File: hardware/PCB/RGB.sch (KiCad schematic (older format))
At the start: 24 parts, among them U1 IS31FL3733-QFLS4-TR, U2 IS31FL3733-QFLS4-TR

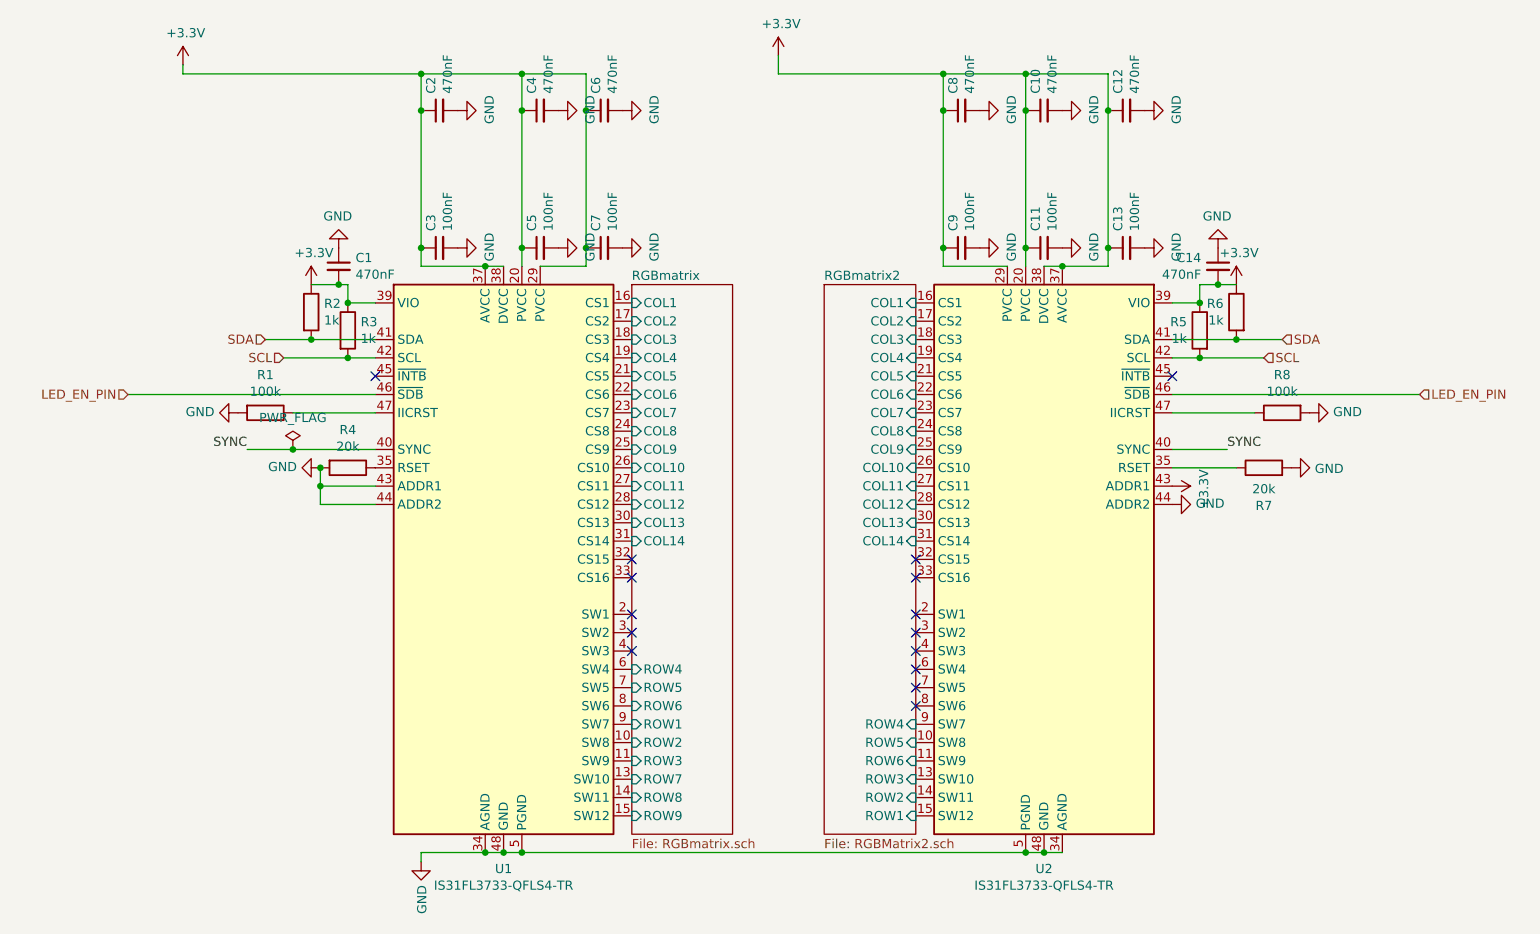
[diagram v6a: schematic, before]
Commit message: fix major issues about the I2C pull up, add in debug
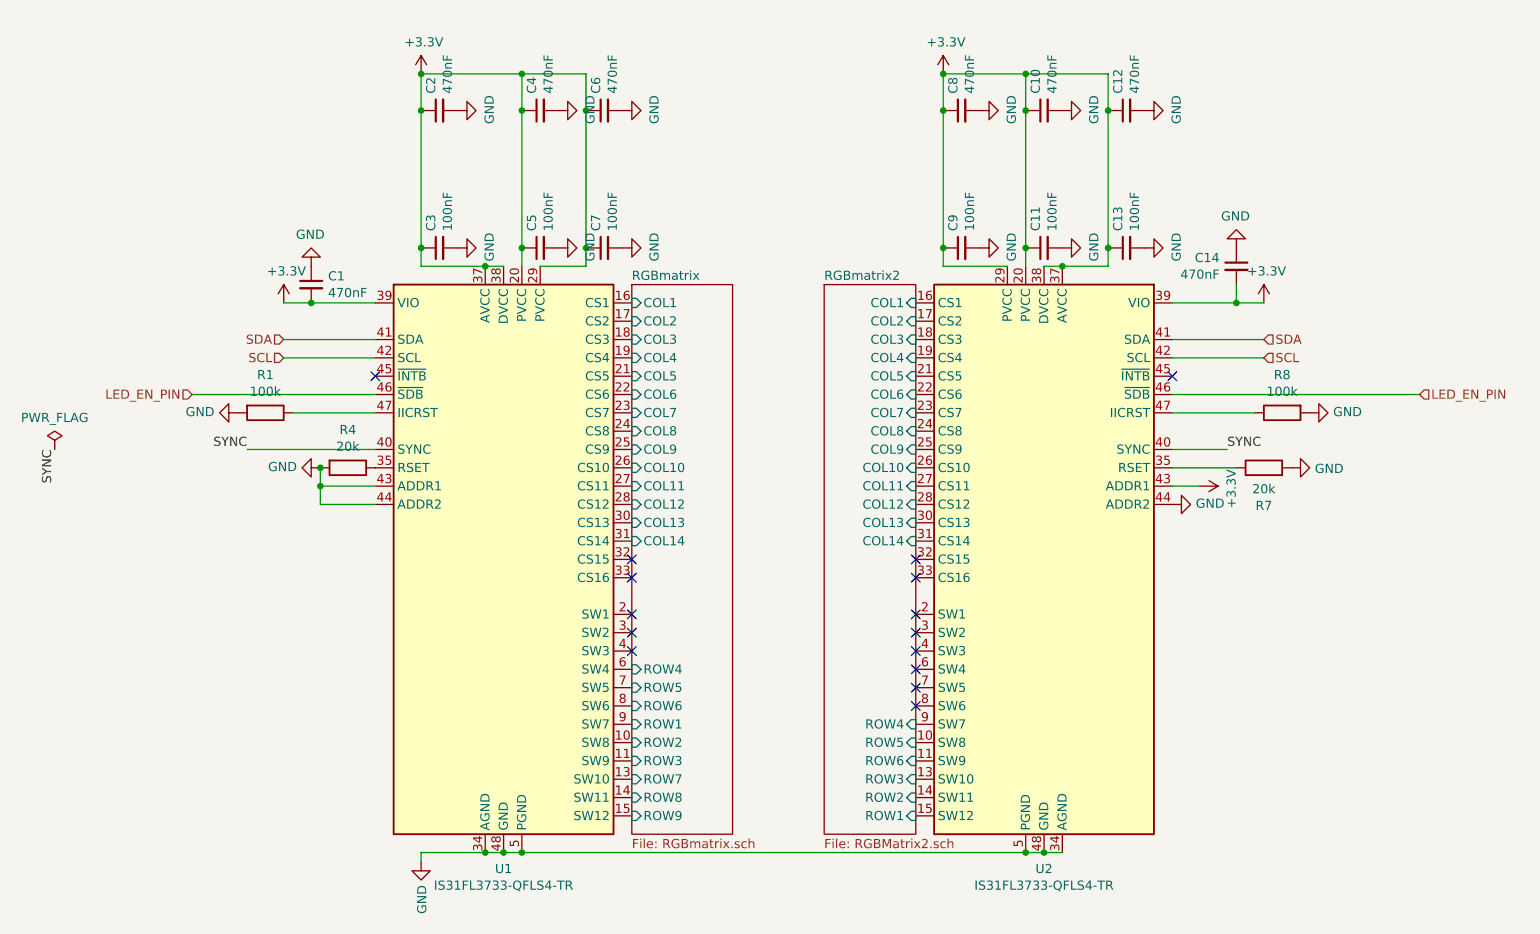
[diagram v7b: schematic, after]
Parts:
- removed R2, R3, R5, R6: 1k, Resistor_SMD:R_0402_1005Metric, symbol Device:R
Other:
- moved on the sheet: C1, C14
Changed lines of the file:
@@
 Text HLabel 8300 2500 2    50   Input ~ 0
 SCL
-Text HLabel 8400 2400 2    50   Input ~ 0
+Text HLabel 8300 2400 2    50   Input ~ 0
 SDA
-Wire Wire Line
-	8400 2400 8150 2400
-Wire Wire Line
-	8150 2400 7800 2400
 Text HLabel 2950 2500 0    50   Input ~ 0
 SCL
-Text HLabel 2850 2400 0    50   Input ~ 0
+Text HLabel 2950 2400 0    50   Input ~ 0
 SDA
 $Comp
@@
 L power:GND #PWR05
 U 1 1 5E42BB66
-P 3250 1900
-F 0 "#PWR05" H 3250 1650 50  0001 C CNN
-F 1 "GND" H 3255 1727 50  0000 C CNN
-F 2 "" H 3250 1900 50  0001 C CNN
-F 3 "" H 3250 1900 50  0001 C CNN
-	1    3250 1900
+P 3100 2000
+F 0 "#PWR05" H 3100 1750 50  0001 C CNN
+F 1 "GND" H 3105 1827 50  0000 C CNN
+F 2 "" H 3100 2000 50  0001 C CNN
+F 3 "" H 3100 2000 50  0001 C CNN
+	1    3100 2000
 	-1   0    0    1
 $EndComp
@@
 L power:GND #PWR022
 U 1 1 5E42518F
-P 8050 1900
-F 0 "#PWR022" H 8050 1650 50  0001 C CNN
-F 1 "GND" H 8055 1727 50  0000 C CNN
-F 2 "" H 8050 1900 50  0001 C CNN
-F 3 "" H 8050 1900 50  0001 C CNN
-	1    8050 1900
+P 8150 1900
+F 0 "#PWR022" H 8150 1650 50  0001 C CNN
+F 1 "GND" H 8155 1727 50  0000 C CNN
+F 2 "" H 8150 1900 50  0001 C CNN
+F 3 "" H 8150 1900 50  0001 C CNN
+	1    8150 1900
 	-1   0    0    1
 $EndComp
@@
 L Device:C_Small C14
 U 1 1 5E406F19
-P 8050 2000
-F 0 "C14" H 8142 2046 50  0000 L CNN
-F 1 "470nF" H 8142 1955 50  0000 L CNN
-F 2 "Capacitor_SMD:C_0402_1005Metric" H 8050 2000 50  0001 C CNN
-F 3 "~" H 8050 2000 50  0001 C CNN
-	1    8050 2000
+P 8150 2000
+F 0 "C14" H 8242 2046 50  0000 L CNN
+F 1 "470nF" H 8242 1955 50  0000 L CNN
+F 2 "Capacitor_SMD:C_0402_1005Metric" H 8150 2000 50  0001 C CNN
+F 3 "~" H 8150 2000 50  0001 C CNN
+	1    8150 2000
 	-1   0    0    -1
 $EndComp
-Connection ~ 7950 2200
-Wire Wire Line
-	7950 2200 7800 2200
-Wire Wire Line
-	7950 2100 7950 2200
-Wire Wire Line
-	8150 2100 8050 2100
-Wire Wire Line
-	7950 2500 8300 2500
-Connection ~ 7950 2500
-$Comp
-L Device:R R5
-U 1 1 5E406F08
-P 7950 2350
-F 0 "R5" H 8020 2396 50  0000 L CNN
-F 1 "1k" H 8020 2305 50  0000 L CNN
-F 2 "Resistor_SMD:R_0402_1005Metric" V 7880 2350 50  0001 C CNN
-F 3 "~" H 7950 2350 50  0001 C CNN
-	1    7950 2350
-	-1   0    0    -1
-$EndComp
-Connection ~ 8150 2400
-$Comp
-L Device:R R6
-U 1 1 5E406EFC
-P 8150 2250
-F 0 "R6" H 8220 2296 50  0000 L CNN
-F 1 "1k" H 8220 2205 50  0000 L CNN
-F 2 "Resistor_SMD:R_0402_1005Metric" V 8080 2250 50  0001 C CNN
-F 3 "~" H 8150 2250 50  0001 C CNN
-	1    8150 2250
-	-1   0    0    -1
-$EndComp
-Wire Wire Line
-	7800 2500 7950 2500
 NoConn ~ 7800 2600
 Wire Wire Line
@@
 NoConn ~ 6400 3700
 NoConn ~ 4850 3700
-Wire Wire Line
-	3250 2100 3300 2100
-Connection ~ 3250 2100
+Connection ~ 3100 2200
 $Comp
 L Device:C_Small C1
 U 1 1 5E39D02A
-P 3250 2000
-F 0 "C1" H 3342 2046 50  0000 L CNN
-F 1 "470nF" H 3342 1955 50  0000 L CNN
-F 2 "Capacitor_SMD:C_0402_1005Metric" H 3250 2000 50  0001 C CNN
-F 3 "~" H 3250 2000 50  0001 C CNN
-	1    3250 2000
+P 3100 2100
+F 0 "C1" H 3192 2146 50  0000 L CNN
+F 1 "470nF" H 3192 2055 50  0000 L CNN
+F 2 "Capacitor_SMD:C_0402_1005Metric" H 3100 2100 50  0001 C CNN
+F 3 "~" H 3100 2100 50  0001 C CNN
+	1    3100 2100
 	1    0    0    -1
 $EndComp
-Connection ~ 3300 2200
-Wire Wire Line
-	3300 2200 3450 2200
 Wire Wire Line
 	4150 5200 4050 5200
@@
 $EndComp
 Wire Wire Line
-	3300 2100 3300 2200
-Wire Wire Line
-	3100 2100 3250 2100
-$Comp
-L Device:R R3
-U 1 1 5E3993FB
-P 3300 2350
-F 0 "R3" H 3370 2396 50  0000 L CNN
-F 1 "1k" H 3370 2305 50  0000 L CNN
-F 2 "Resistor_SMD:R_0402_1005Metric" V 3230 2350 50  0001 C CNN
-F 3 "~" H 3300 2350 50  0001 C CNN
-	1    3300 2350
-	1    0    0    -1
-$EndComp
-$Comp
-L Device:R R2
-U 1 1 5E398E31
-P 3100 2250
-F 0 "R2" H 3170 2296 50  0000 L CNN
-F 1 "1k" H 3170 2205 50  0000 L CNN
-F 2 "Resistor_SMD:R_0402_1005Metric" V 3030 2250 50  0001 C CNN
-F 3 "~" H 3100 2250 50  0001 C CNN
-	1    3100 2250
-	1    0    0    -1
-$EndComp
+	2950 2200 3100 2200
 NoConn ~ 3450 2600
 Wire Wire Line
@@
 Wire Wire Line
 	4600 2000 4350 2000
-Text HLabel 2100 2700 0    50   Input ~ 0
+Text HLabel 2450 2700 0    50   Input ~ 0
 LED_EN_PIN
 Text HLabel 9150 2700 2    50   Input ~ 0
 LED_EN_PIN
-Wire Wire Line
-	3450 2400 3100 2400
-Connection ~ 3100 2400
-Wire Wire Line
-	3100 2400 2850 2400
-Wire Wire Line
-	2950 2500 3300 2500
-Connection ~ 3300 2500
-Wire Wire Line
-	3300 2500 3450 2500
-Wire Wire Line
-	5650 950  6550 950
 Text Label 2750 3000 2    50   ~ 0
 SYNC
@@
 Wire Wire Line
 	8100 3000 7800 3000
-Wire Wire Line
-	2750 3000 3000 3000
 $Comp
 L power:PWR_FLAG #FLG01
 U 1 1 5E6BEB0B
-P 3000 3000
-F 0 "#FLG01" H 3000 3075 50  0001 C CNN
-F 1 "PWR_FLAG" H 3000 3173 50  0000 C CNN
-F 2 "" H 3000 3000 50  0001 C CNN
-F 3 "~" H 3000 3000 50  0001 C CNN
-	1    3000 3000
+P 1700 3000
+F 0 "#FLG01" H 1700 3075 50  0001 C CNN
+F 1 "PWR_FLAG" H 1700 3173 50  0000 C CNN
+F 2 "" H 1700 3000 50  0001 C CNN
+F 3 "~" H 1700 3000 50  0001 C CNN
+	1    1700 3000
 	1    0    0    -1
 $EndComp
-Connection ~ 3000 3000
-Wire Wire Line
-	3000 3000 3450 3000
-Wire Wire Line
-	5650 850  5650 950
-Wire Wire Line
-	2400 900  2400 950
-Connection ~ 3700 950
 Connection ~ 3700 1900
 Wire Wire Line
@@
 Wire Wire Line
 	4600 1150 4600 1900
-Wire Wire Line
-	2400 950  3700 950
 Connection ~ 6550 1900
 Wire Wire Line
@@
 Wire Wire Line
 	7450 1900 7450 2000
-Connection ~ 8050 2100
-Wire Wire Line
-	7950 2100 8050 2100
 Wire Wire Line
 	8150 3100 7800 3100
@@
 	7450 1150 7450 1900
 $Comp
-L power:+3.3V #PWR01
-U 1 1 5E275074
-P 2400 900
-F 0 "#PWR01" H 2400 750 50  0001 C CNN
-F 1 "+3.3V" H 2415 1073 50  0000 C CNN
-F 2 "" H 2400 900 50  0001 C CNN
-F 3 "" H 2400 900 50  0001 C CNN
-	1    2400 900
-	1    0    0    -1
-$EndComp
-$Comp
 L power:+3.3V #PWR03
 U 1 1 5E277141
-P 3100 2100
-F 0 "#PWR03" H 3100 1950 50  0001 C CNN
-F 1 "+3.3V" H 3115 2273 50  0000 C CNN
-F 2 "" H 3100 2100 50  0001 C CNN
-F 3 "" H 3100 2100 50  0001 C CNN
-	1    3100 2100
+P 2950 2200
+F 0 "#PWR03" H 2950 2050 50  0001 C CNN
+F 1 "+3.3V" H 2965 2373 50  0000 C CNN
+F 2 "" H 2950 2200 50  0001 C CNN
+F 3 "" H 2950 2200 50  0001 C CNN
+	1    2950 2200
 	1    0    0    -1
 $EndComp
@@
 L power:+3.3V #PWR013
 U 1 1 5E27A2F2
-P 5650 850
-F 0 "#PWR013" H 5650 700 50  0001 C CNN
-F 1 "+3.3V" H 5665 1023 50  0000 C CNN
-F 2 "" H 5650 850 50  0001 C CNN
-F 3 "" H 5650 850 50  0001 C CNN
-	1    5650 850
+P 6550 950
+F 0 "#PWR013" H 6550 800 50  0001 C CNN
+F 1 "+3.3V" H 6565 1123 50  0000 C CNN
+F 2 "" H 6550 950 50  0001 C CNN
+F 3 "" H 6550 950 50  0001 C CNN
+	1    6550 950
 	1    0    0    -1
 $EndComp
@@
 L power:+3.3V #PWR023
 U 1 1 5E27D7A3
-P 8150 2100
-F 0 "#PWR023" H 8150 1950 50  0001 C CNN
-F 1 "+3.3V" H 8165 2273 50  0000 C CNN
-F 2 "" H 8150 2100 50  0001 C CNN
-F 3 "" H 8150 2100 50  0001 C CNN
-	1    8150 2100
+P 8300 2200
+F 0 "#PWR023" H 8300 2050 50  0001 C CNN
+F 1 "+3.3V" H 8315 2373 50  0000 C CNN
+F 2 "" H 8300 2200 50  0001 C CNN
+F 3 "" H 8300 2200 50  0001 C CNN
+	1    8300 2200
 	1    0    0    -1
 $EndComp
@@
 L power:+3.3V #PWR020
 U 1 1 5E280F4E
-P 7800 3200
-F 0 "#PWR020" H 7800 3050 50  0001 C CNN
-F 1 "+3.3V" H 7815 3373 50  0000 C CNN
-F 2 "" H 7800 3200 50  0001 C CNN
-F 3 "" H 7800 3200 50  0001 C CNN
-	1    7800 3200
+P 7950 3200
+F 0 "#PWR020" H 7950 3050 50  0001 C CNN
+F 1 "+3.3V" H 7965 3373 50  0000 C CNN
+F 2 "" H 7950 3200 50  0001 C CNN
+F 3 "" H 7950 3200 50  0001 C CNN
+	1    7950 3200
 	0    1    1    0
 $EndComp
@@
 Wire Wire Line
 	7800 2700 9150 2700
-Wire Wire Line
-	2100 2700 3450 2700
 NoConn ~ 4850 4100
 NoConn ~ 4850 4000
@@
 F21 "ROW6" I R 6400 4700 50
 $EndSheet
+Wire Wire Line
+	2950 2500 3450 2500
+Wire Wire Line
+	7950 3200 7800 3200
+Wire Wire Line
+	3450 2400 2950 2400
+Wire Wire Line
+	7800 2500 8300 2500
+Wire Wire Line
+	3100 2200 3450 2200
+$Comp
+L power:+3.3V #PWR01
+U 1 1 5E275074
+P 3700 950
+F 0 "#PWR01" H 3700 800 50  0001 C CNN
+F 1 "+3.3V" H 3715 1123 50  0000 C CNN
+F 2 "" H 3700 950 50  0001 C CNN
+F 3 "" H 3700 950 50  0001 C CNN
+	1    3700 950
+	1    0    0    -1
+$EndComp
+Connection ~ 3700 950
+Wire Wire Line
+	8300 2400 7800 2400
+Wire Wire Line
+	7800 2200 8150 2200
+Wire Wire Line
+	8150 2200 8150 2100
+Connection ~ 8150 2200
+Wire Wire Line
+	8150 2200 8300 2200
+Wire Wire Line
+	3450 2700 2450 2700
+Wire Wire Line
+	2750 3000 3450 3000
+Text Label 1700 3000 3    50   ~ 0
+SYNC
 $EndSCHEMATC
